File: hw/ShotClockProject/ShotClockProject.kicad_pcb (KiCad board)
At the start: 2 copper layers, 94 parts, among them IC1 TP4056-42-ESOP8_Rearanged, J1 USB4120-03-C_REVA, J10 DW254W-22-20-85, J2 Conn_ST_STDC14, J3 Conn_01x06_Pin, J4 Conn_01x03_Pin, J5 Conn_01x02_Pin, J6 Conn_01x03_Pin, J7 DW254W-22-20-85, J8 DW254W-22-20-85, J9 DW254W-22-20-85, Q1 Q_NPN_BCE, Q2 Q_PMOS_SGD, SW1 SW_SPDT, SW2 SW_SPDT, SW3 SW_SPST, SW4 SW_SPST, SW5 SW_SPST, U1 STM32F103RCT6, U2 LD39015M33R, U3 TPS63000, U4 M74HC14YRM13TR, Y1 16MHz

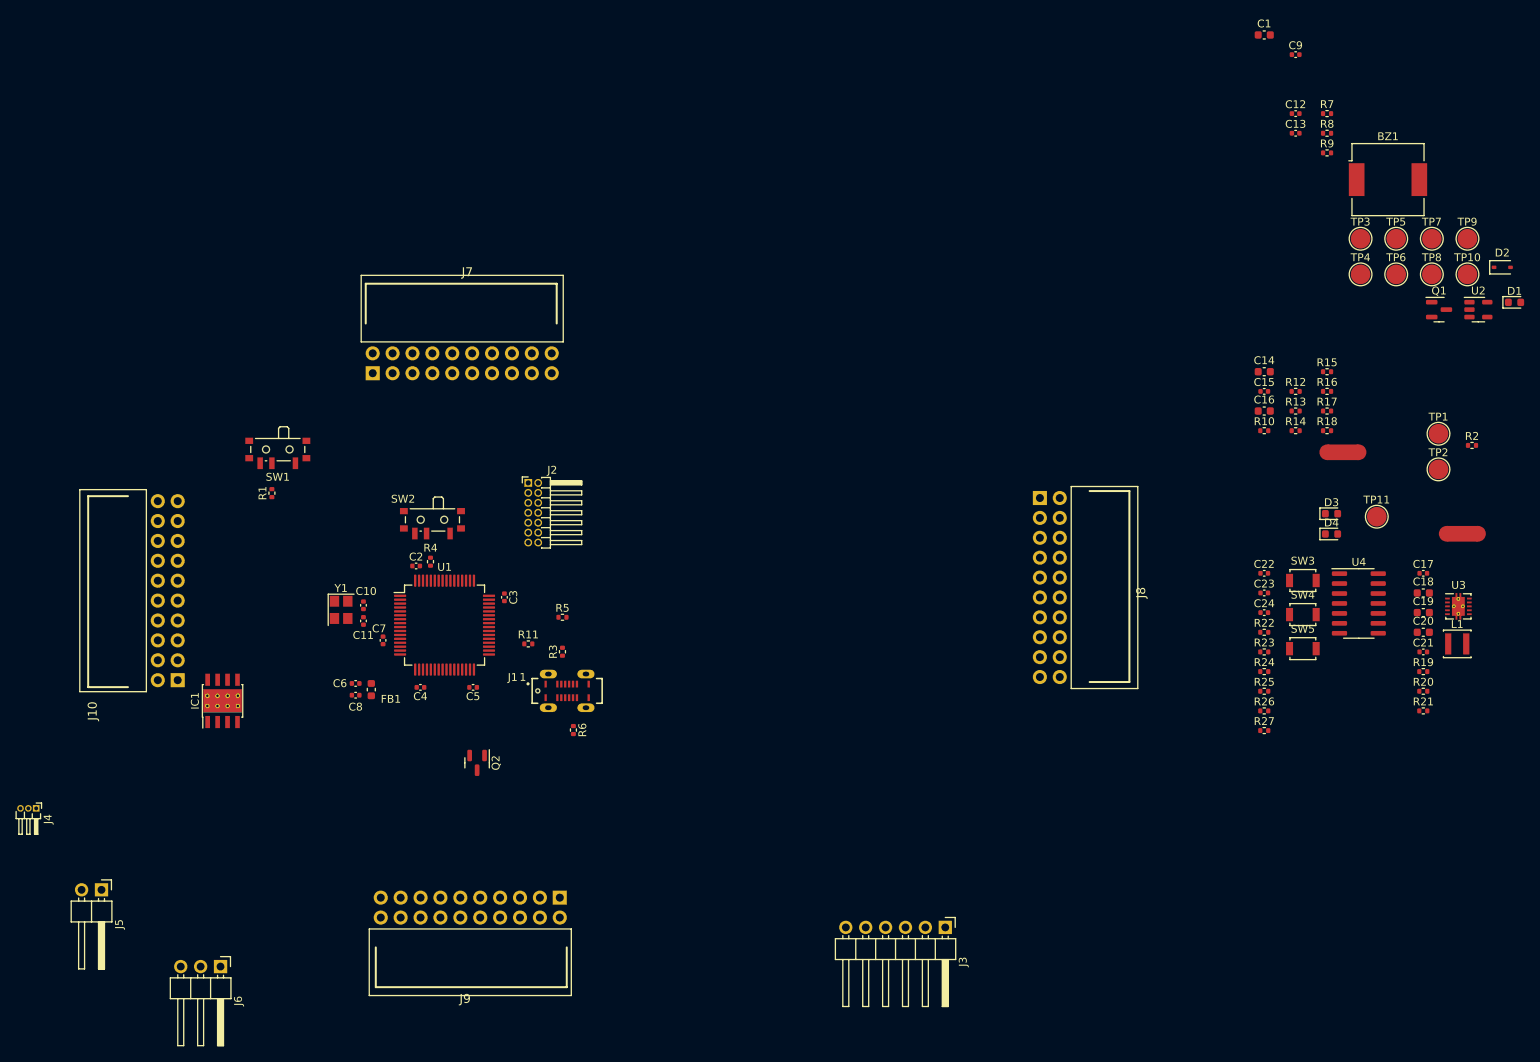
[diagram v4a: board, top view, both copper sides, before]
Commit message: Finished rough layout of PCB (ready for review)
Changed battery polarity to match the batteries I have.
Added power led to voltage regulator
Removed old comments from schematic
Gave all footprints a 3D model
Replaced batttery footprint with a SMD JST 3 pins horizontal connector
Finished rough placement of components
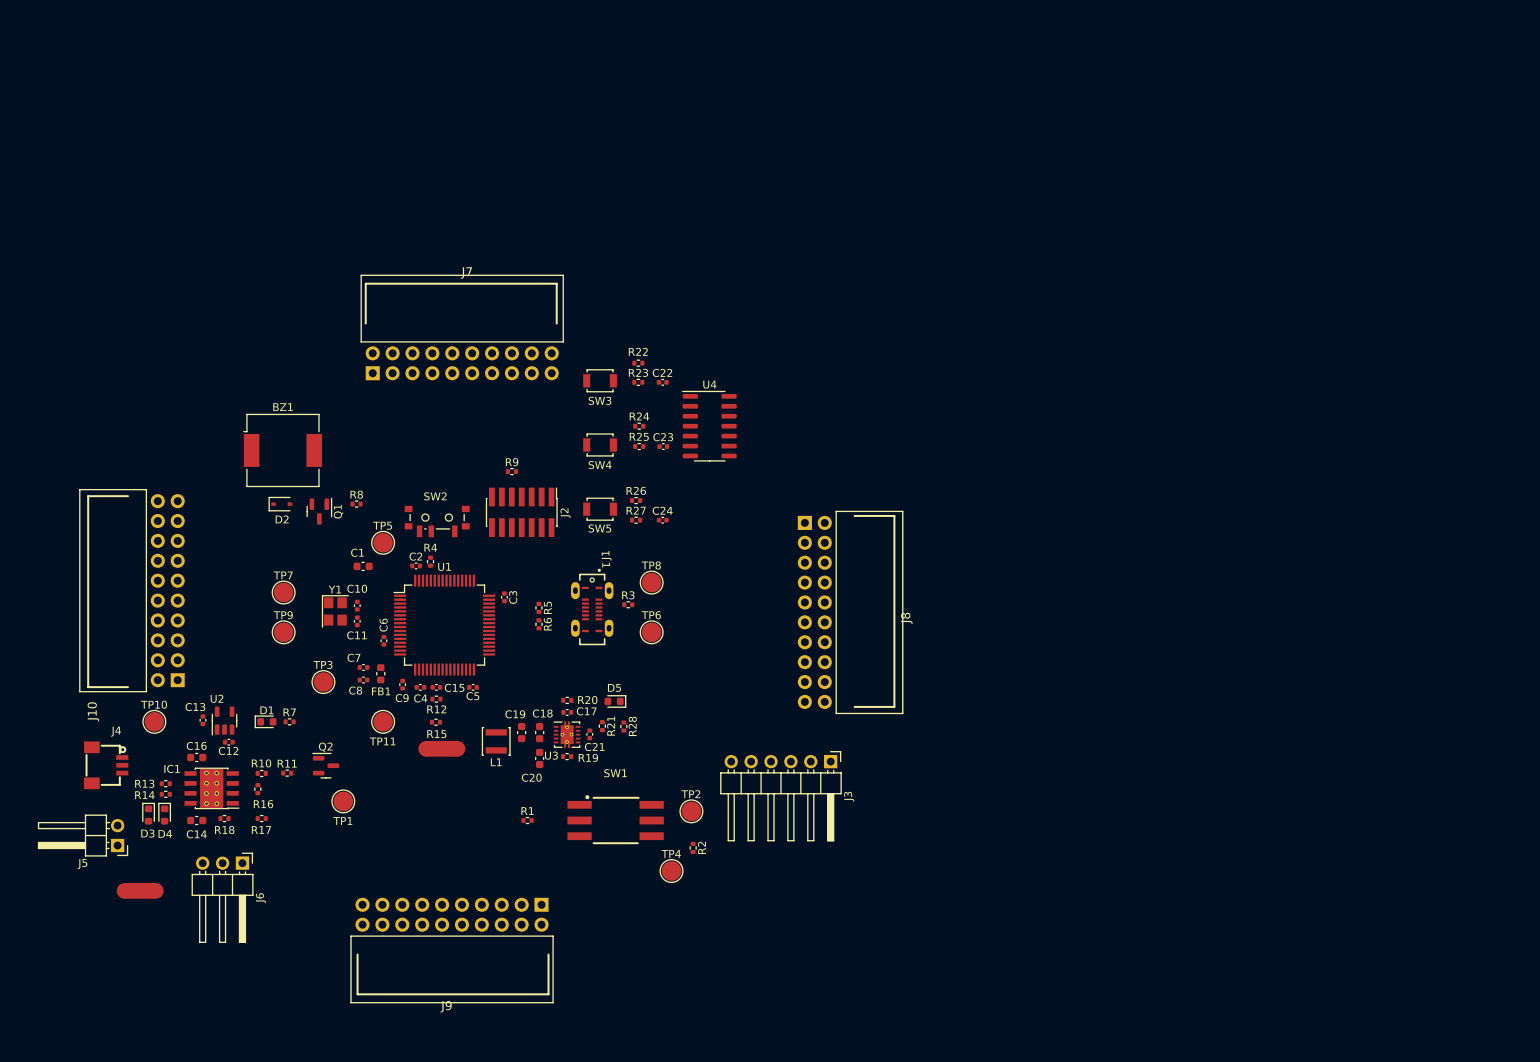
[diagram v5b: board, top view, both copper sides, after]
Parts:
- added D5: G_LED, LED_SMD:LED_0603_1608Metric, F.Cu at (169.2, 105.3)
- added R28: 1k5, Resistor_SMD:R_0402_1005Metric, F.Cu at (170.4, 108.5)
- J2: footprint Connector_PinHeader_1.27mm:PinHeader_2x07_P1.27mm_Horizontal -> Connector_PinHeader_1.27mm:PinHeader_2x07_P1.27mm_Vertical_SMD
- J4: value Conn_01x03_Pin -> SM03B-SRSS-TB(LF)(SN)(P); footprint Connector_PinHeader_1.00mm:PinHeader_1x03_P1.00mm_Horizontal -> SM03B-SRSS-TB:CONN-SMD_SM03B-SRSS-TB-LF-SN-P
- SW1: value SW_SPDT -> PS-5824SVB-6PL; footprint Button_Switch_SMD:SW_SPDT_PCM12 -> PS-5824SVB-6PL:SW-SMD_6P-L5.8-W5.8-P2.00-LS11.3
- SW2: footprint Button_Switch_SMD:SW_SPDT_PCM12 -> Button_Switch_SMD_Altered:SW_SPDT_PCM12_Upwards
- U3: footprint Package_SON:Texas_DRC0010J_ThermalVias -> Package_SON_Altered:Texas_DRC0010J_ThermalVias_Altered
- moved TP10 177.1 mm to (110.5, 108.0)
- moved U2 168.5 mm to (119.5, 107.8), turned to 90 degrees
- moved D1 168.1 mm to (124.9, 108.0)
- moved NT1 163.5 mm to (108.7, 129.5), turned to 180 degrees
- moved TP9 159.3 mm to (127.0, 96.5)
- moved D2 158.8 mm to (126.8, 80.2)
- moved C13 158.4 mm to (116.7, 107.8), turned to -90 degrees
- moved C12 158.1 mm to (120.0, 110.5), turned to 180 degrees
- moved D3 155.9 mm to (109.8, 119.8), turned to -90 degrees
- moved R7 153.6 mm to (127.8, 108.0)
- moved TP7 153.4 mm to (127.0, 91.4)
- moved D4 153.3 mm to (111.8, 119.8), turned to -90 degrees
- moved R13 151.9 mm to (112.0, 115.8)
- moved R14 151.6 mm to (112.0, 117.2)
- moved R18 149.2 mm to (119.5, 120.3)
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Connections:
- C17 pad 1: /Voltage regulator 3v3/3v3_out -> Net-(D5-A)
- C18 pad 1: /Voltage regulator 3v3/3v3_out -> Net-(D5-A)
- C19 pad 1: /Voltage regulator 3v3/3v3_out -> Net-(D5-A)
- J4 pad 1: +BATT -> -BATT
- J4 pad 3: -BATT -> +BATT
- J5 pad 1: +BATT -> -BATT
- J5 pad 2: -BATT -> +BATT
- R20 pad 1: /Voltage regulator 3v3/3v3_out -> Net-(D5-A)
- U3 pad 1: /Voltage regulator 3v3/3v3_out -> Net-(D5-A)

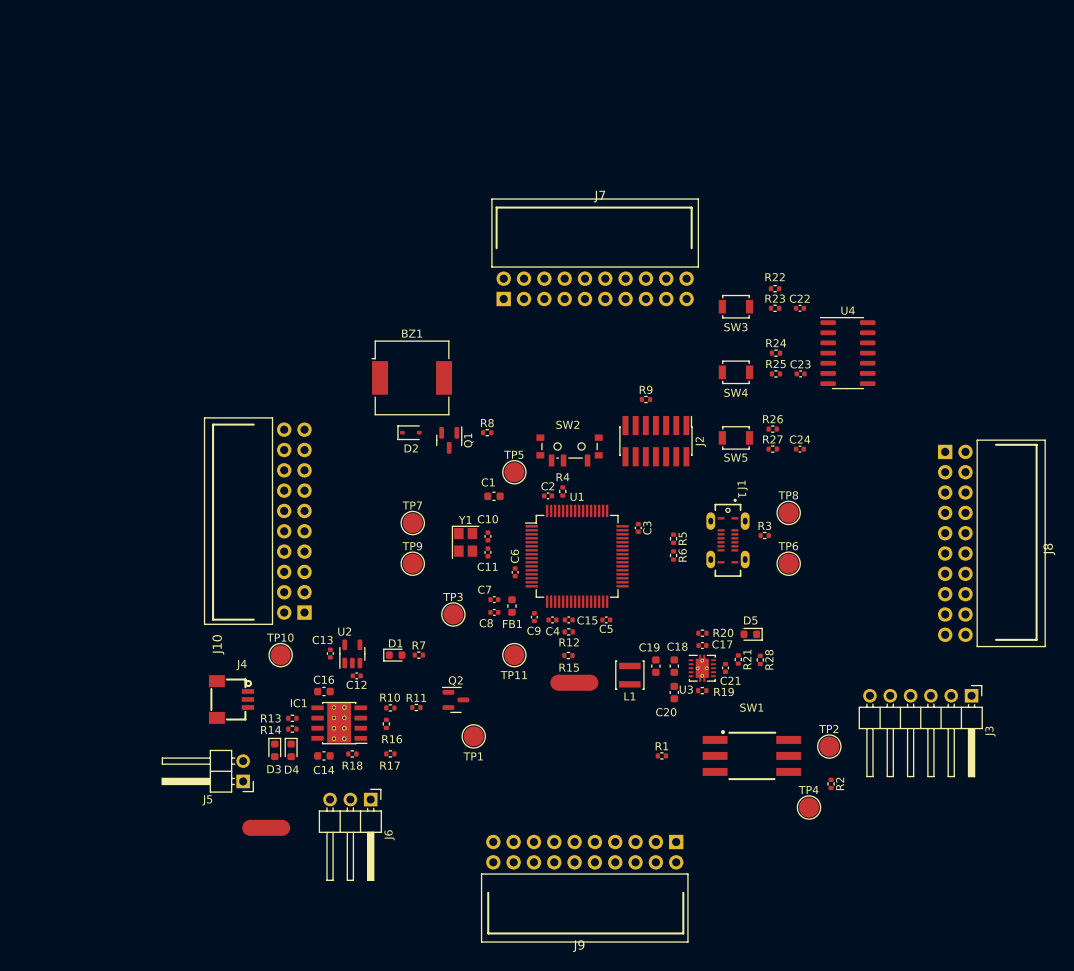
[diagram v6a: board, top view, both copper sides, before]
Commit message: Added footprint for MOSFET and updated PCB
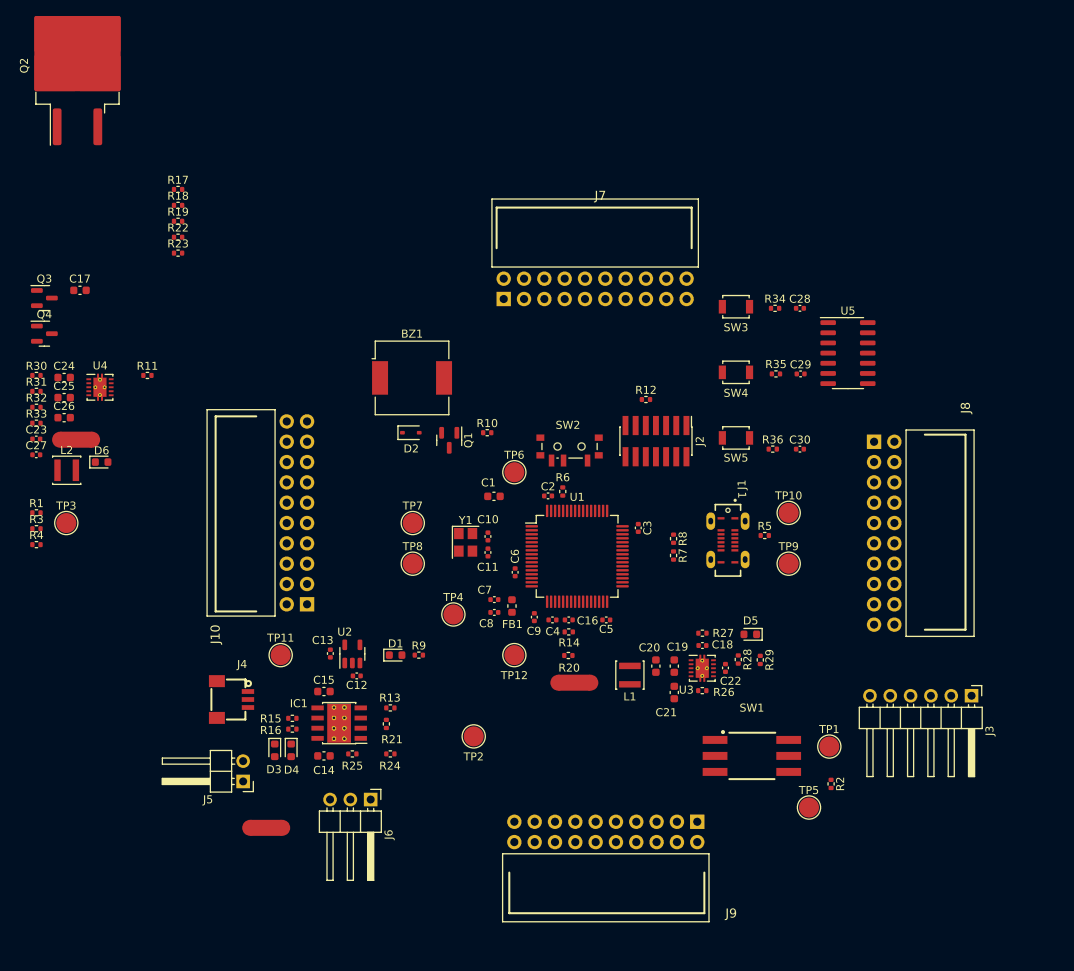
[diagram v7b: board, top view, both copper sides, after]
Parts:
- removed the R24 at (172.4, 70.2)
- removed the R26 at (172.0, 79.7)
- added C17: 10n, Capacitor_SMD:C_0603_1608Metric, F.Cu at (85.4, 62.4)
- added C23: 2.2p, Capacitor_SMD:C_0402_1005Metric, F.Cu at (79.9, 80.9)
- added C24: 10u, Capacitor_SMD:C_0603_1608Metric, F.Cu at (83.4, 73.2)
- added C25: 10u, Capacitor_SMD:C_0603_1608Metric, F.Cu at (83.4, 75.8)
- added C26: 10u, Capacitor_SMD:C_0603_1608Metric, F.Cu at (83.4, 78.3)
- added C27: 0.1u, Capacitor_SMD:C_0402_1005Metric, F.Cu at (79.9, 82.9)
- added D6: G_LED, LED_SMD:LED_0603_1608Metric, F.Cu at (88.1, 83.8)
- added L2: 2.2uH, Inductor_SMD:L_Sunlord_SWPA3012S, F.Cu at (83.7, 84.8)
- added NT3: NetTie_2, NetTie:NetTie-2_SMD_Pad2.0mm, F.Cu at (84.9, 81.0)
- added Q3: Q_NPN_BCE, Package_TO_SOT_SMD:SOT-23, F.Cu at (81.0, 63.3)
- added Q4: Q_NPN_BCE, Package_TO_SOT_SMD:SOT-23, F.Cu at (81.0, 67.8)
- added R17: 1k, Resistor_SMD:R_0402_1005Metric, F.Cu at (97.7, 49.7)
- added R18: 1k, Resistor_SMD:R_0402_1005Metric, F.Cu at (97.7, 51.7)
- added R19: 100k, Resistor_SMD:R_0402_1005Metric, F.Cu at (97.7, 53.7)
- added R23: 10k, Resistor_SMD:R_0402_1005Metric, F.Cu at (97.7, 57.7)
- added R3: 0R, Resistor_SMD:R_0402_1005Metric, F.Cu at (80.0, 92.2)
- added R30: 100R, Resistor_SMD:R_0402_1005Metric, F.Cu at (80.0, 73.0)
- added R31: 1M, Resistor_SMD:R_0402_1005Metric, F.Cu at (80.0, 75.0)
- added R32: 110k, Resistor_SMD:R_0402_1005Metric, F.Cu at (80.0, 77.0)
- added R33: 1k5, Resistor_SMD:R_0402_1005Metric, F.Cu at (80.0, 79.0)
- added R4: 0R, Resistor_SMD:R_0402_1005Metric, F.Cu at (80.0, 94.1)
- added TP3: TestPoint, TestPoint:TestPoint_Pad_D2.5mm, F.Cu at (83.7, 91.4)
- added U4: TPS63000, Package_SON_Altered:Texas_DRC0010J_ThermalVias_Altered, F.Cu at (87.9, 74.5)
- C10, C11: value 10p -> 6p
- L1: value L -> 2.2uH
- Q2: footprint Package_TO_SOT_SMD:SOT-23 -> Package_TO_SOT_SMD:TO-263-2
- R10: renamed from R8; value 1k -> 300R
- R22: value 47k -> 10k
- moved Q2 92.3 mm to (85.1, 34.3), turned to 90 degrees
- moved R1 83.9 mm to (80.0, 90.2)
- moved R22 74.9 mm to (97.7, 55.7), turned to 0 degrees
- moved R11 53.4 mm to (93.8, 73.0)
- moved J8 8.98 mm to (185.9, 92.7)
- moved J9 3.65 mm to (151.1, 130.1)
- moved J10 1.08 mm to (112.5, 90.2)
- renumbered C16 to C15, C15 to C16, C17 to C18, C18 to C19, C19 to C20, C20 to C21, C21 to C22, C22 to C28, C23 to C29, C24 to C30, R9 to R12, R10 to R13, R12 to R14, R13 to R15, R14 to R16, R15 to R20, R16 to R21, R17 to R24, R18 to R25, R19 to R26, R20 to R27, R21 to R28, R28 to R29, R23 to R34, R25 to R35, R27 to R36, R3 to R5, R4 to R6, R6 to R7, R5 to R8, R7 to R9, TP2 to TP1, TP8 to TP10, TP10 to TP11, TP11 to TP12, TP1 to TP2, TP3 to TP4, TP4 to TP5, TP5 to TP6, TP9 to TP8, TP6 to TP9, U4 to U5
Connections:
- C18 pad 1: Net-(D5-A) -> /Voltage regulator 3v3/3v3_out
- C19 pad 1: Net-(D5-A) -> /Voltage regulator 3v3/3v3_out
- C20 pad 1: Net-(D5-A) -> /Voltage regulator 3v3/3v3_out
- C28 pad 1: Net-(U4-1A) -> Net-(SW3-B)
- C29 pad 1: Net-(U4-2A) -> Net-(SW4-B)
- C30 pad 1: Net-(U4-3A) -> Net-(SW5-B)
- D5 pad 1: /Voltage regulator 3v3/3v3_out -> Net-(D5-K)
- D5 pad 2: Net-(D5-A) -> /Voltage regulator 3v3/3v3_out
- J10 pad 1: +3.3V -> +5V
- J10 pad 10: /Connectors to segment displays/PWM12_TIM4_CH4 -> /Connectors to segment displays/DISP2_SEG_A
- J10 pad 11: /Connectors to segment displays/PWM5_TIM3_CH1 -> /Connectors to segment displays/DISP2_SEG_B
- J10 pad 12: /Connectors to segment displays/PWM13_TIM5_CH1 -> /Connectors to segment displays/DISP2_SEG_C
- J10 pad 13: /Connectors to segment displays/PWM6_TIM3_CH2 -> /Connectors to segment displays/DISP2_SEG_D
- J10 pad 14: /Connectors to segment displays/PWM14_TIM5_CH2 -> /Connectors to segment displays/DISP2_SEG_E
- J10 pad 15: /Connectors to segment displays/PWM7_TIM3_CH3 -> /Connectors to segment displays/DISP2_SEG_F
- J10 pad 16: /Connectors to segment displays/PWM15_TIM5_CH3 -> /Connectors to segment displays/DISP2_SEG_G
- J10 pad 17: /Connectors to segment displays/PWM8_TIM3_CH4 -> /Connectors to segment displays/DISP2_SEG_DP
- J10 pad 18: /Connectors to segment displays/PWM16_TIM5_CH4 -> /Connectors to segment displays/TIM2_CH1_PWM1_SEG
- J10 pad 2: GND -> /Connectors to segment displays/DISP1_SEG_A
- J10 pad 20: GND -> /Connectors to segment displays/TIM2_CH2_PWM2_SEG
- J10 pad 3: /Connectors to segment displays/PWM1_TIM2_CH1 -> /Connectors to segment displays/DISP1_SEG_B
- J10 pad 4: /Connectors to segment displays/PWM9_TIM4_CH1 -> /Connectors to segment displays/DISP1_SEG_C
- J10 pad 5: /Connectors to segment displays/PWM2_TIM2_CH2 -> /Connectors to segment displays/DISP1_SEG_D
- J10 pad 6: /Connectors to segment displays/PWM10_TIM4_CH2 -> /Connectors to segment displays/DISP1_SEG_E
- J10 pad 7: /Connectors to segment displays/PWM3_TIM2_CH3 -> /Connectors to segment displays/DISP1_SEG_F
- J10 pad 8: /Connectors to segment displays/PWM11_TIM4_CH3 -> /Connectors to segment displays/DISP1_SEG_G
- J10 pad 9: /Connectors to segment displays/PWM4_TIM2_CH4 -> /Connectors to segment displays/DISP1_SEG_DP
- J7 pad 1: +3.3V -> +5V
- J7 pad 10: /Connectors to segment displays/PWM12_TIM4_CH4 -> /Connectors to segment displays/DISP2_SEG_A
- J7 pad 11: /Connectors to segment displays/PWM5_TIM3_CH1 -> /Connectors to segment displays/DISP2_SEG_B
- J7 pad 12: /Connectors to segment displays/PWM13_TIM5_CH1 -> /Connectors to segment displays/DISP2_SEG_C
- J7 pad 13: /Connectors to segment displays/PWM6_TIM3_CH2 -> /Connectors to segment displays/DISP2_SEG_D
- J7 pad 14: /Connectors to segment displays/PWM14_TIM5_CH2 -> /Connectors to segment displays/DISP2_SEG_E
- J7 pad 15: /Connectors to segment displays/PWM7_TIM3_CH3 -> /Connectors to segment displays/DISP2_SEG_F
- J7 pad 16: /Connectors to segment displays/PWM15_TIM5_CH3 -> /Connectors to segment displays/DISP2_SEG_G
- J7 pad 17: /Connectors to segment displays/PWM8_TIM3_CH4 -> /Connectors to segment displays/DISP2_SEG_DP
- J7 pad 18: /Connectors to segment displays/PWM16_TIM5_CH4 -> /Connectors to segment displays/TIM2_CH1_PWM1_SEG
- J7 pad 2: GND -> /Connectors to segment displays/DISP1_SEG_A
- J7 pad 20: GND -> /Connectors to segment displays/TIM2_CH2_PWM2_SEG
- J7 pad 3: /Connectors to segment displays/PWM1_TIM2_CH1 -> /Connectors to segment displays/DISP1_SEG_B
- J7 pad 4: /Connectors to segment displays/PWM9_TIM4_CH1 -> /Connectors to segment displays/DISP1_SEG_C
- J7 pad 5: /Connectors to segment displays/PWM2_TIM2_CH2 -> /Connectors to segment displays/DISP1_SEG_D
- J7 pad 6: /Connectors to segment displays/PWM10_TIM4_CH2 -> /Connectors to segment displays/DISP1_SEG_E
- J7 pad 7: /Connectors to segment displays/PWM3_TIM2_CH3 -> /Connectors to segment displays/DISP1_SEG_F
- J7 pad 8: /Connectors to segment displays/PWM11_TIM4_CH3 -> /Connectors to segment displays/DISP1_SEG_G
- J7 pad 9: /Connectors to segment displays/PWM4_TIM2_CH4 -> /Connectors to segment displays/DISP1_SEG_DP
- J8 pad 1: +3.3V -> +5V
- J8 pad 10: /Connectors to segment displays/PWM12_TIM4_CH4 -> /Connectors to segment displays/DISP2_SEG_A
- J8 pad 11: /Connectors to segment displays/PWM5_TIM3_CH1 -> /Connectors to segment displays/DISP2_SEG_B
- J8 pad 12: /Connectors to segment displays/PWM13_TIM5_CH1 -> /Connectors to segment displays/DISP2_SEG_C
- J8 pad 13: /Connectors to segment displays/PWM6_TIM3_CH2 -> /Connectors to segment displays/DISP2_SEG_D
- J8 pad 14: /Connectors to segment displays/PWM14_TIM5_CH2 -> /Connectors to segment displays/DISP2_SEG_E
- J8 pad 15: /Connectors to segment displays/PWM7_TIM3_CH3 -> /Connectors to segment displays/DISP2_SEG_F
- J8 pad 16: /Connectors to segment displays/PWM15_TIM5_CH3 -> /Connectors to segment displays/DISP2_SEG_G
- J8 pad 17: /Connectors to segment displays/PWM8_TIM3_CH4 -> /Connectors to segment displays/DISP2_SEG_DP
- J8 pad 18: /Connectors to segment displays/PWM16_TIM5_CH4 -> /Connectors to segment displays/TIM2_CH1_PWM1_SEG
- J8 pad 2: GND -> /Connectors to segment displays/DISP1_SEG_A
- J8 pad 20: GND -> /Connectors to segment displays/TIM2_CH2_PWM2_SEG
- J8 pad 3: /Connectors to segment displays/PWM1_TIM2_CH1 -> /Connectors to segment displays/DISP1_SEG_B
- J8 pad 4: /Connectors to segment displays/PWM9_TIM4_CH1 -> /Connectors to segment displays/DISP1_SEG_C
- J8 pad 5: /Connectors to segment displays/PWM2_TIM2_CH2 -> /Connectors to segment displays/DISP1_SEG_D
- J8 pad 6: /Connectors to segment displays/PWM10_TIM4_CH2 -> /Connectors to segment displays/DISP1_SEG_E
- J8 pad 7: /Connectors to segment displays/PWM3_TIM2_CH3 -> /Connectors to segment displays/DISP1_SEG_F
- J8 pad 8: /Connectors to segment displays/PWM11_TIM4_CH3 -> /Connectors to segment displays/DISP1_SEG_G
- J8 pad 9: /Connectors to segment displays/PWM4_TIM2_CH4 -> /Connectors to segment displays/DISP1_SEG_DP
- J9 pad 1: +3.3V -> +5V
- J9 pad 10: /Connectors to segment displays/PWM12_TIM4_CH4 -> /Connectors to segment displays/DISP2_SEG_A
- J9 pad 11: /Connectors to segment displays/PWM5_TIM3_CH1 -> /Connectors to segment displays/DISP2_SEG_B
- J9 pad 12: /Connectors to segment displays/PWM13_TIM5_CH1 -> /Connectors to segment displays/DISP2_SEG_C
- J9 pad 13: /Connectors to segment displays/PWM6_TIM3_CH2 -> /Connectors to segment displays/DISP2_SEG_D
- J9 pad 14: /Connectors to segment displays/PWM14_TIM5_CH2 -> /Connectors to segment displays/DISP2_SEG_E
- J9 pad 15: /Connectors to segment displays/PWM7_TIM3_CH3 -> /Connectors to segment displays/DISP2_SEG_F
- J9 pad 16: /Connectors to segment displays/PWM15_TIM5_CH3 -> /Connectors to segment displays/DISP2_SEG_G
- J9 pad 17: /Connectors to segment displays/PWM8_TIM3_CH4 -> /Connectors to segment displays/DISP2_SEG_DP
- J9 pad 18: /Connectors to segment displays/PWM16_TIM5_CH4 -> /Connectors to segment displays/TIM2_CH1_PWM1_SEG
- J9 pad 2: GND -> /Connectors to segment displays/DISP1_SEG_A
- J9 pad 20: GND -> /Connectors to segment displays/TIM2_CH2_PWM2_SEG
- J9 pad 3: /Connectors to segment displays/PWM1_TIM2_CH1 -> /Connectors to segment displays/DISP1_SEG_B
- J9 pad 4: /Connectors to segment displays/PWM9_TIM4_CH1 -> /Connectors to segment displays/DISP1_SEG_C
- J9 pad 5: /Connectors to segment displays/PWM2_TIM2_CH2 -> /Connectors to segment displays/DISP1_SEG_D
- J9 pad 6: /Connectors to segment displays/PWM10_TIM4_CH2 -> /Connectors to segment displays/DISP1_SEG_E
- J9 pad 7: /Connectors to segment displays/PWM3_TIM2_CH3 -> /Connectors to segment displays/DISP1_SEG_F
- J9 pad 8: /Connectors to segment displays/PWM11_TIM4_CH3 -> /Connectors to segment displays/DISP1_SEG_G
- J9 pad 9: /Connectors to segment displays/PWM4_TIM2_CH4 -> /Connectors to segment displays/DISP1_SEG_DP
- R1 pad 1: /Li-Po Battery and charger/charger_out -> Net-(R1-Pad1)
- R1 pad 2: Net-(R1-Pad2) -> /Voltage regulator 3v3/batt_in
- R10 pad 2: /STM32F103RCT6/BUZZER -> /STM32F103RCT6/PWM3_BUZZER
- R11 pad 1: VBUS -> GND
- R11 pad 2: Net-(Q2-G) -> Net-(Q1-B)
- R22 pad 1: +3.3V -> GND
- R22 pad 2: Net-(SW3-A) -> Net-(Q3-B)
- R27 pad 1: Net-(D5-A) -> /Voltage regulator 3v3/3v3_out
- R29 pad 1: /Voltage regulator 3v3/3v3_out -> Net-(D5-K)
- R34 pad 1: Net-(SW3-A) -> GND
- R34 pad 2: Net-(U4-1A) -> Net-(SW3-B)
- R35 pad 1: Net-(SW4-A) -> GND
- R35 pad 2: Net-(U4-2A) -> Net-(SW4-B)
- R36 pad 1: Net-(SW5-A) -> GND
- R36 pad 2: Net-(U4-3A) -> Net-(SW5-B)
- SW1 pad 2: Net-(R1-Pad2) -> /Li-Po Battery and charger/charger_out
- SW1 pad 3: /Voltage regulator 3v3/batt_in -> Net-(R1-Pad1)
- SW3 pad 1: Net-(SW3-A) -> +3.3V
- SW3 pad 2: GND -> Net-(SW3-B)
- SW4 pad 1: Net-(SW4-A) -> +3.3V
- SW4 pad 2: GND -> Net-(SW4-B)
- SW5 pad 1: Net-(SW5-A) -> +3.3V
- SW5 pad 2: GND -> Net-(SW5-B)
- U1 pad 14: /Connectors to segment displays/PWM13_TIM5_CH1 -> /Connectors to segment displays/DISP1_SEG_A
- U1 pad 15: /Connectors to segment displays/PWM14_TIM5_CH2 -> /Connectors to segment displays/DISP1_SEG_B
- U1 pad 16: /Connectors to segment displays/PWM15_TIM5_CH3 -> /Connectors to segment displays/DISP1_SEG_C
- U1 pad 17: /Connectors to segment displays/PWM16_TIM5_CH4 -> /Connectors to segment displays/DISP1_SEG_D
- U1 pad 21: unconnected-(U1-PA5-Pad21) -> /Connectors to segment displays/DISP1_SEG_E
- U1 pad 22: /Connectors to segment displays/PWM5_TIM3_CH1 -> /Connectors to segment displays/DISP1_SEG_F
- U1 pad 23: /Connectors to segment displays/PWM6_TIM3_CH2 -> /Connectors to segment displays/DISP1_SEG_G
- U1 pad 26: /Connectors to segment displays/PWM7_TIM3_CH3 -> /Connectors to segment displays/DISP2_SEG_A
- U1 pad 27: /Connectors to segment displays/PWM8_TIM3_CH4 -> /Connectors to segment displays/DISP2_SEG_B
- U1 pad 28: unconnected-(U1-PB2-Pad28) -> /Connectors to segment displays/DISP2_SEG_C
- U1 pad 29: /Connectors to segment displays/PWM3_TIM2_CH3 -> unconnected-(U1-PB10-Pad29)
- U1 pad 30: /Connectors to segment displays/PWM4_TIM2_CH4 -> unconnected-(U1-PB11-Pad30)
- U1 pad 37: unconnected-(U1-PC6-Pad37) -> /STM32F103RCT6/PWM3_BUZZER
- U1 pad 4: /STM32F103RCT6/BUZZER -> unconnected-(U1-PC15-Pad4)
- U1 pad 41: unconnected-(U1-PA8-Pad41) -> /Connectors to segment displays/DISP1_SEG_DP
- U1 pad 50: /Connectors to segment displays/PWM1_TIM2_CH1 -> /Connectors to segment displays/TIM2_CH1_PWM1_SEG
- U1 pad 55: /Connectors to segment displays/PWM2_TIM2_CH2 -> /Connectors to segment displays/TIM2_CH2_PWM2_SEG
- U1 pad 56: unconnected-(U1-PB4-Pad56) -> /Connectors to segment displays/DISP2_SEG_D
- U1 pad 57: unconnected-(U1-PB5-Pad57) -> /Connectors to segment displays/DISP2_SEG_E
- U1 pad 58: /Connectors to segment displays/PWM9_TIM4_CH1 -> /Connectors to segment displays/DISP2_SEG_F
- U1 pad 59: /Connectors to segment displays/PWM10_TIM4_CH2 -> /Connectors to segment displays/DISP2_SEG_G
- U1 pad 61: /Connectors to segment displays/PWM11_TIM4_CH3 -> /Connectors to segment displays/DISP2_SEG_DP
- U1 pad 62: /Connectors to segment displays/PWM12_TIM4_CH4 -> unconnected-(U1-PB9-Pad62)
- U3 pad 1: Net-(D5-A) -> /Voltage regulator 3v3/3v3_out
- U5 pad 1: Net-(U4-1A) -> Net-(SW3-B)
- U5 pad 3: Net-(U4-2A) -> Net-(SW4-B)
- U5 pad 5: Net-(U4-3A) -> Net-(SW5-B)
